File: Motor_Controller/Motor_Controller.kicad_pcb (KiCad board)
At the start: 2 copper layers, 68 x 38 mm, 33 parts, among them J1 I/O, Q1 DMG4800LK3, Q2 DMG4800LK3, Q3 DMG4800LK3, Q4 DMG4800LK3, U1 LTC7060IMSE, U2 LTC7060IMSE, U3 LM358, U4 RT9064-50GV, U5 PI4ULS5V201TAEX

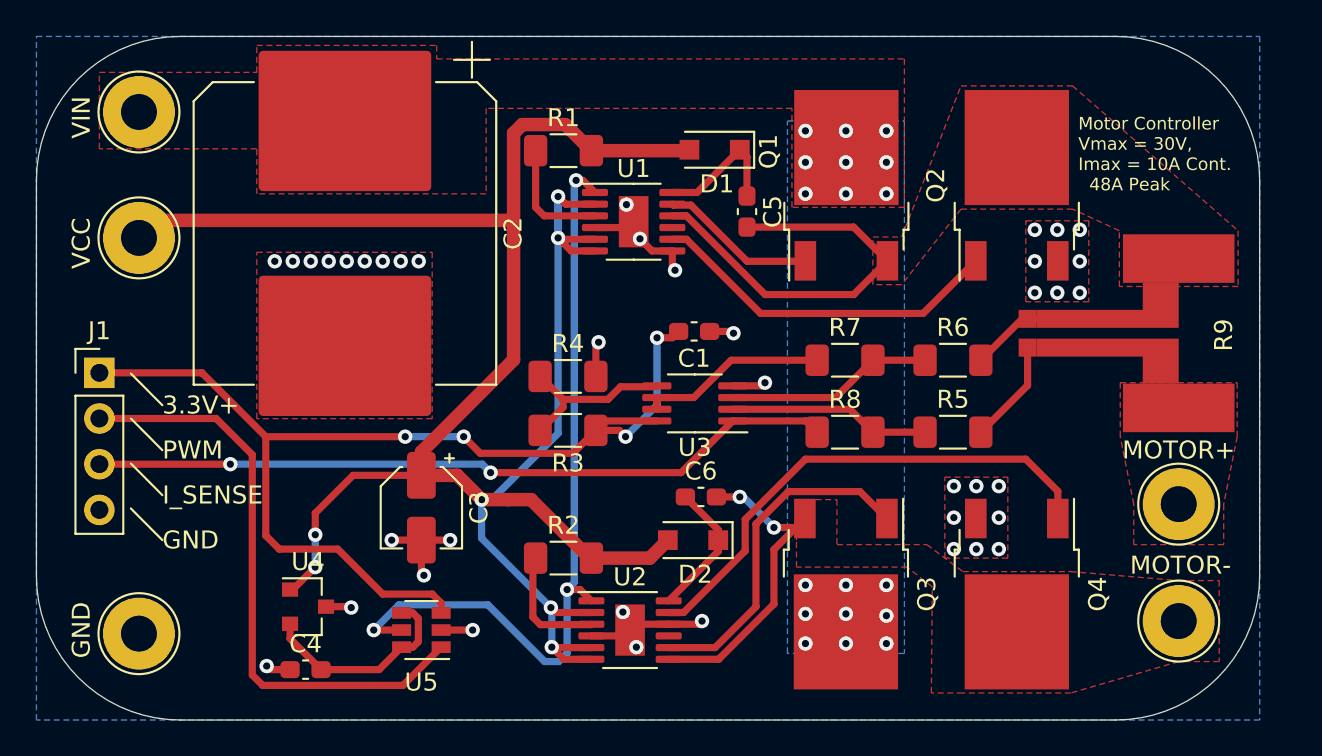
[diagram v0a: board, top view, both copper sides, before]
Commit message: Updated Motor Controller
Added 100V Functionality, Changed MOSFET (100V, 70A), Changed Diode (100V 2A), Changed Capacitor (100V 100uF, D10mm, P5mm) and changed to in-stock op-amp LM358AWST
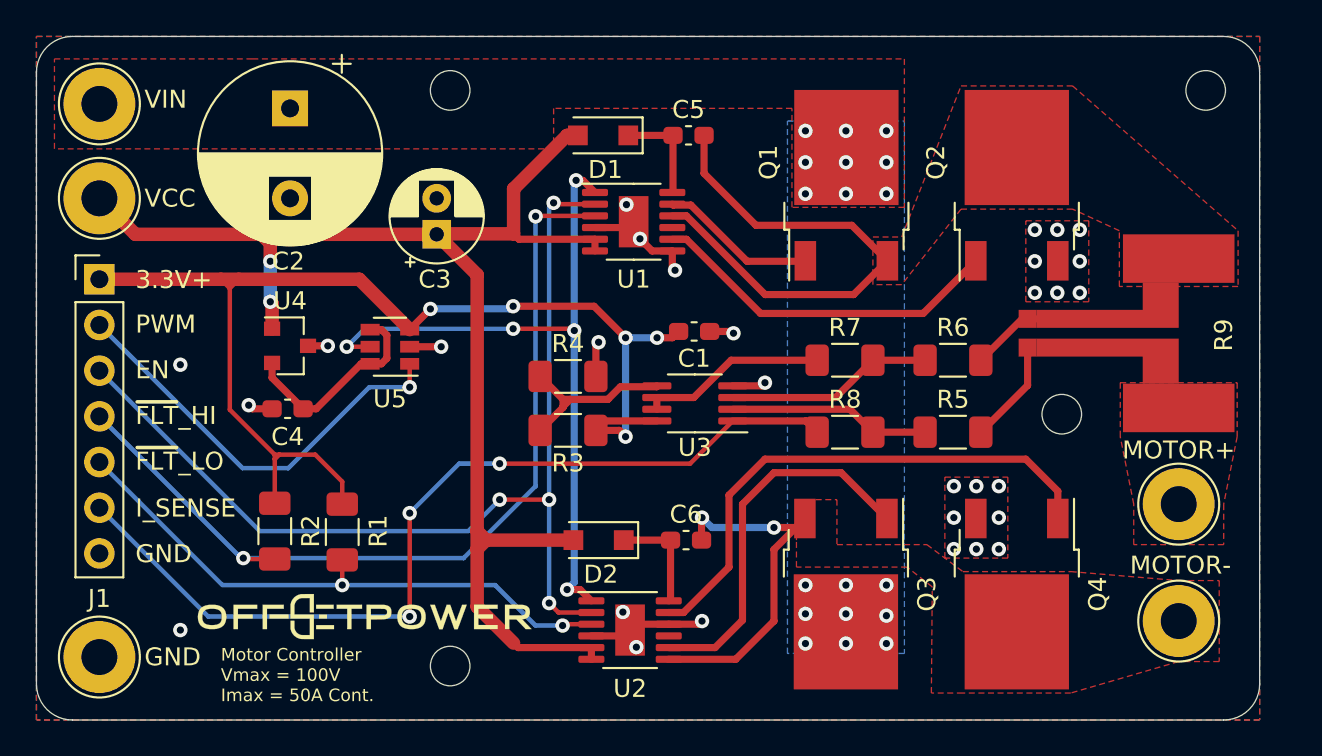
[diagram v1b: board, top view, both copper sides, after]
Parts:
- removed the G*** at (47.5, 126.8)
- added G***: LOGO, Project_Library:pcb_logo_20_6x6_3mm, F.Cu at (42.2, 155.2)
- added H1: MountingHole, MountingHole:MountingHole_2.2mm_M2, F.Cu at (81.0, 144.0)
- added H2: MountingHole, MountingHole:MountingHole_2.2mm_M2, F.Cu at (47.0, 158.0)
- added H3: MountingHole, MountingHole:MountingHole_2.2mm_M2, F.Cu at (47.0, 126.0)
- added H4: MountingHole, MountingHole:MountingHole_2.2mm_M2, F.Cu at (89.0, 126.0)
- C2: value 470U -> 100U; footprint Capacitor_SMD:CP_Elec_16x22 -> Capacitor_THT:CP_Radial_D10.0mm_P5.00mm
- C3: footprint Capacitor_SMD:CP_Elec_4x5.4 -> Capacitor_THT:CP_Radial_D5.0mm_P2.00mm
- J1: value I/O -> Conn_01x06; footprint Connector_PinHeader_2.54mm:PinHeader_1x04_P2.54mm_Vertical -> Connector_PinHeader_2.54mm:PinHeader_1x07_P2.54mm_Vertical
- Q1, Q2, Q3, Q4: value DMG4800LK3 -> FDD86250-F085‎
- moved R1 24.5 mm to (41.0, 150.6), turned to 90 degrees
- moved R2 16.1 mm to (37.2, 150.5), turned to 90 degrees
- moved U5 15.8 mm to (43.6, 140.2)
- moved C3 15.2 mm to (46.2, 134.0), turned to 90 degrees
- moved C4 14.5 mm to (38.0, 143.7)
- moved U4 14.5 mm to (38.1, 140.2)
- moved C2 7.59 mm to (38.1, 127.0)
- moved D1 6.25 mm to (55.5, 128.5)
- moved C5 5.34 mm to (60.2, 128.5), turned to 0 degrees
- moved D2 5.25 mm to (55.2, 151.0)
- moved J1 5.20 mm to (27.5, 136.5)
- moved TP3 3.11 mm to (27.5, 132.0)
- moved TP4 2.56 mm to (27.5, 157.5)
- moved C6 2.54 mm to (60.1, 151.0)
- moved TP5 2.25 mm to (27.5, 126.8)
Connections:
- J1 pad 3: I_SENSE -> EN
- J1 pad 4: GND -> ~FLT~_HI
- R1 pad 1: Net-(R1-Pad1) -> ~FLT~_LO
- R1 pad 2: VCC -> +3V3
- R2 pad 1: Net-(R2-Pad1) -> ~FLT~_HI
- R2 pad 2: VCC -> +3V3
- U1 pad 2: VCC -> EN
- U1 pad 3: Net-(R1-Pad1) -> ~FLT~_HI
- U2 pad 2: VCC -> EN
- U2 pad 3: Net-(R2-Pad1) -> ~FLT~_LO
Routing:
- net EN: track 0.00 -> 56.7 mm, vias 0 -> 4
- net ~FLT~_HI: track 0.00 -> 49.3 mm, vias 0 -> 2
- net VCC: track 125.4 -> 79.0 mm, vias 7 -> 2
- net ~FLT~_LO: track 0.00 -> 32.5 mm, vias 0 -> 2
- net PWM_IN: track 33.2 -> 23.7 mm, vias 0 -> 1
- net I_SENSE: track 41.5 -> 50.5 mm, vias 2 -> 3
- net Net-(R2-Pad1): track 6.79 -> 0.00 mm
- net Net-(R1-Pad1): track 6.65 -> 0.00 mm
- net +3V3: track 60.3 -> 66.5 mm, vias 4 -> 5
- net CSR+: track 34.0 -> 39.8 mm
- net GND: track 27.0 -> 21.4 mm, vias 40 -> 30
- net PWM: track 43.8 -> 40.3 mm, vias 3 -> 5
- net Net-(C6-Pad2): track 18.4 -> 20.6 mm
- net Net-(Q3-Pad1): track 19.0 -> 21.0 mm
- net Net-(C5-Pad1): track 7.47 -> 5.68 mm
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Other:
- outline, holes or cut-outs redrawn
- board text added: "EN"
- board text added: "MOTOR CONTROLLER REV. A1"
- board text added: "Motor Controller Vmax = 100V Imax = 50A Cont."
- board text added: "~FLT~_HI"
- board text added: "~FLT~_LO"
- board text removed: "MOTOR CONTROLLER REV. A0"
- board text removed: "Motor Controller Vmax = 30V, Imax = 10A Cont. 48A Peak"
